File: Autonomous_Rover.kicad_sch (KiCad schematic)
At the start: 42 parts, among them J1 VL53L5X_R, J10 ESP32_R, J13 POWER, J14 BEAM_LIGHT, J15 MOTOR, J16 UART_5V, J17 UART_3V, J2 VEML7700, J3 VL53L5X_L, J4 HC-SR04_M, J5 VL53L5X_M, J7 BNO085, J9 ESP32_L, Q1 AO3400A, Q2 AO3400A, U1 AMS1117-3.3

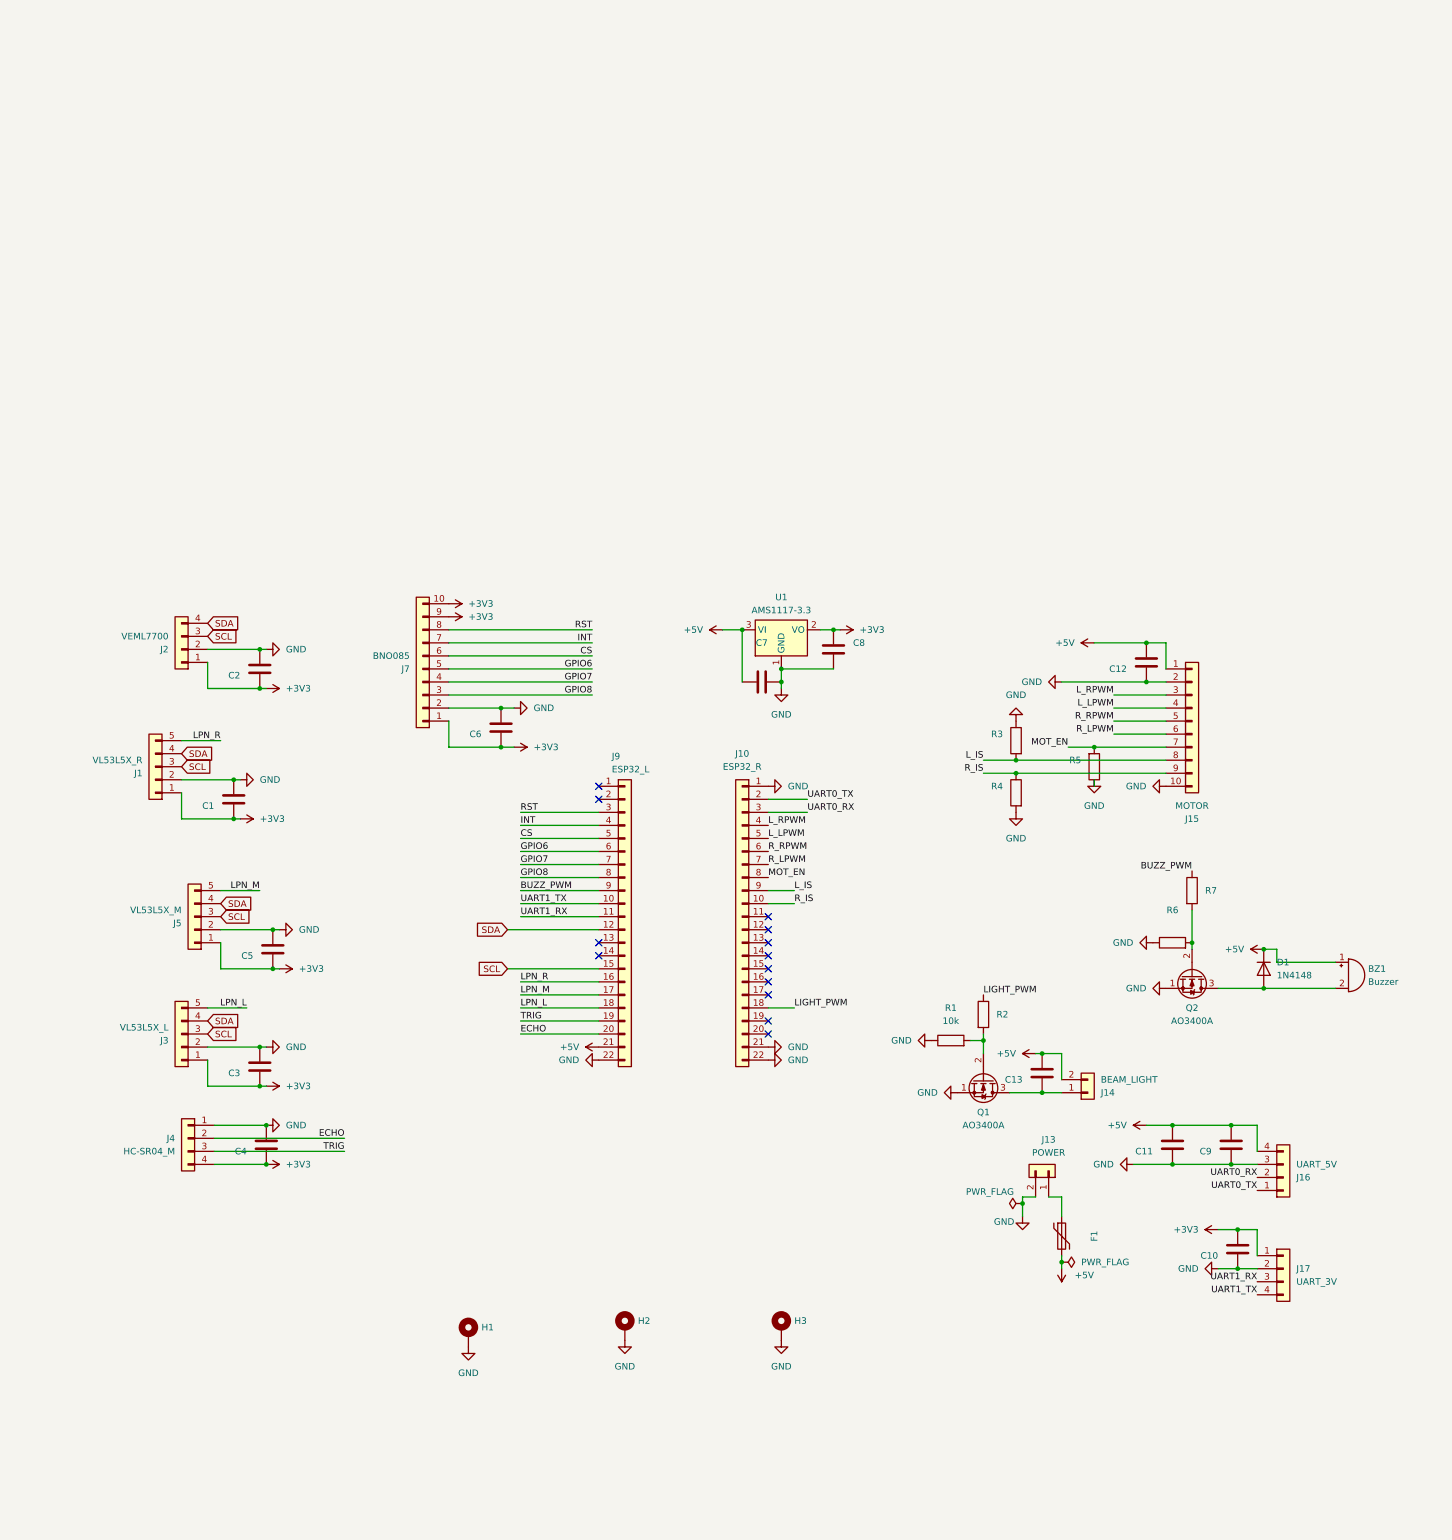
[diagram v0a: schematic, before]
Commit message: Reorganize Schematic
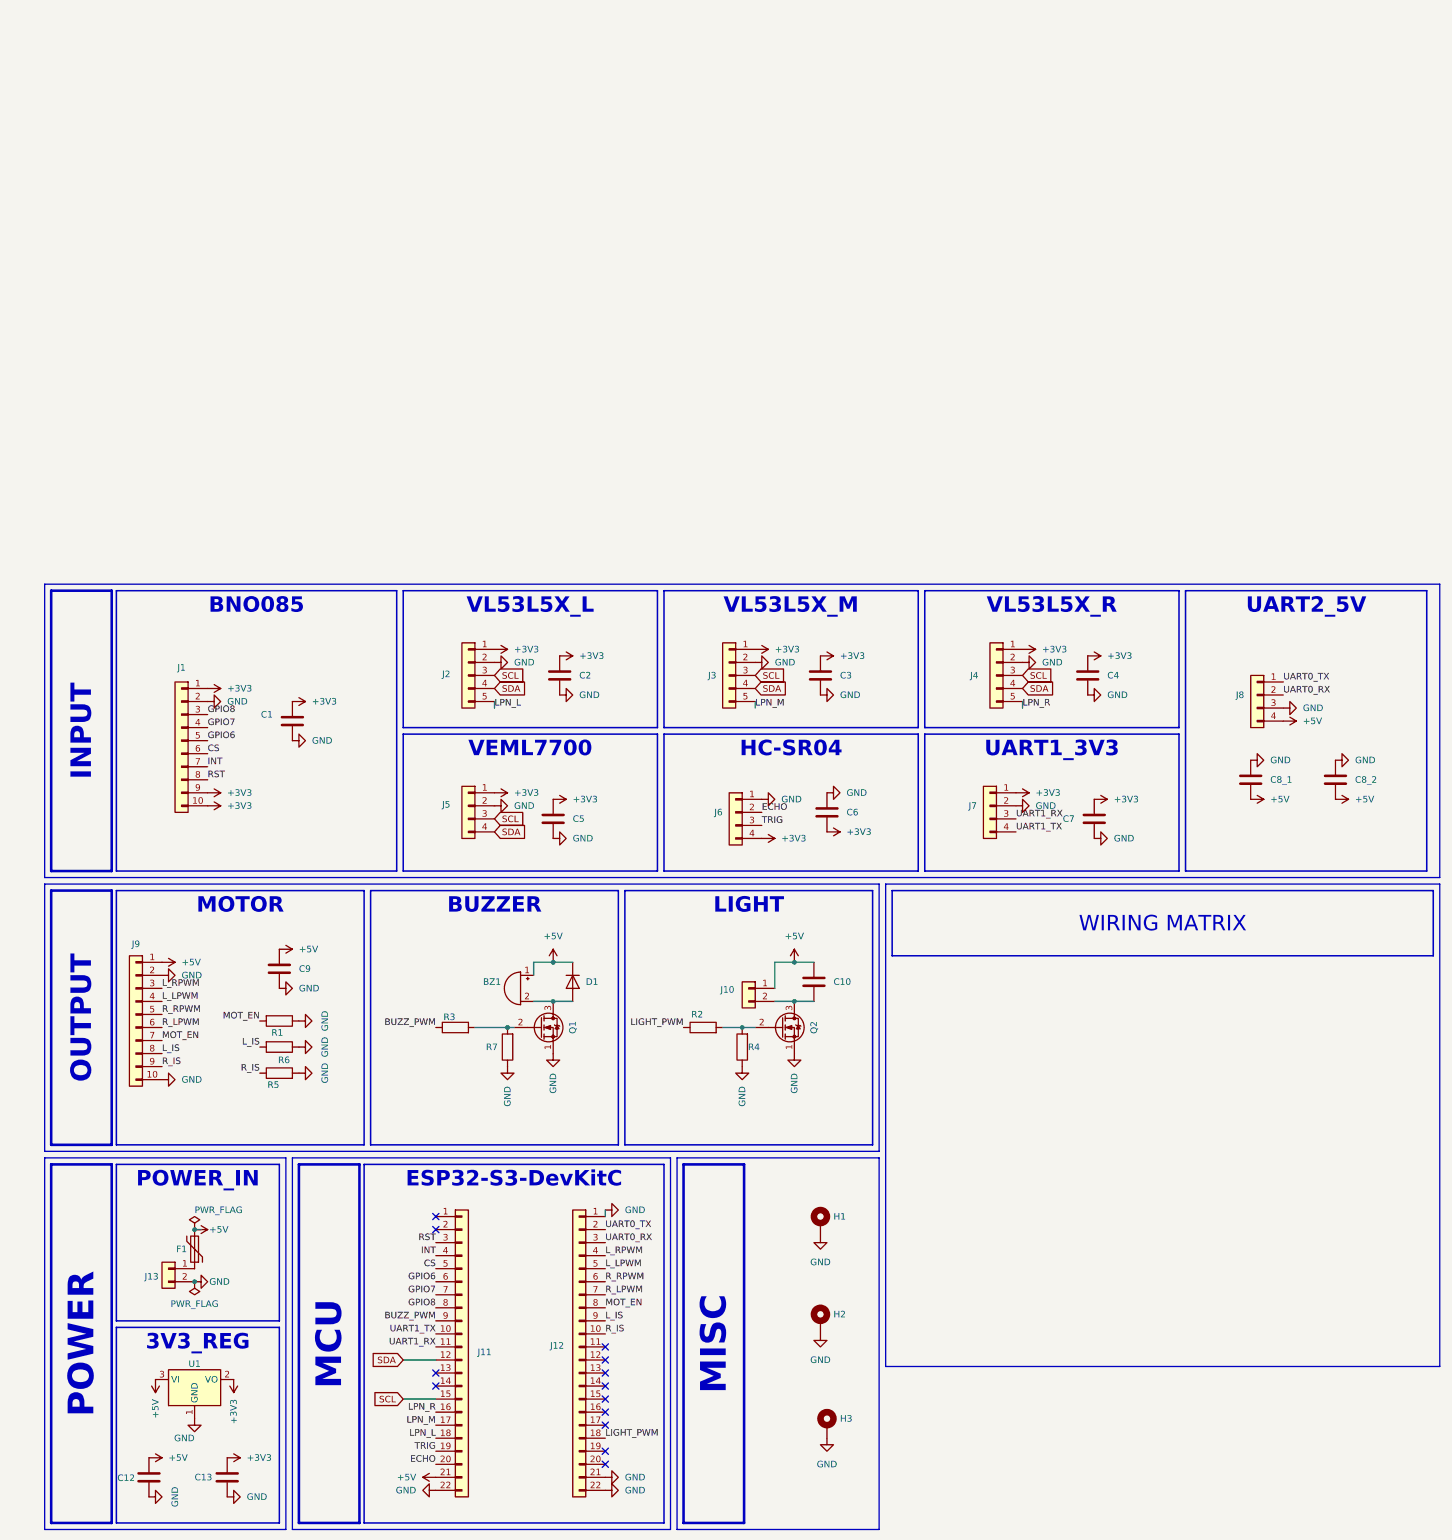
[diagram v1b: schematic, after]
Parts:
- removed C10: 100nF, Capacitor_SMD:C_0805_2012Metric, symbol Device:C
- removed C11, C8: 10uF, Capacitor_SMD:C_0805_2012Metric, symbol Device:C
- removed R3: 1k, Resistor_SMD:R_0805_2012Metric, symbol Device:R
- added C13, C8_2: 10uF, Capacitor_SMD:C_0805_2012Metric, symbol Device:C
- added C8_1: 100nF, Capacitor_SMD:C_0805_2012Metric, symbol Device:C
- added R6: 1k, Resistor_SMD:R_0805_2012Metric, symbol Device:R
- C12: value 100nF -> 10uF
- C7: value 10uF -> 100nF
- R4: value 1k -> 10k
- R5: value 10k -> 1k
- renumbered C13 to C10, J7 to J1, J14 to J10, J9 to J11, J10 to J12, J3 to J2, J5 to J3, J1 to J4, J2 to J5, J4 to J6, J17 to J7, J16 to J8, J15 to J9, R7 to R3, R6 to R7
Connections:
- net +3V3: now also C7.2, C13.1
- net +5V: now also C10.1, C12.1, J10.1 (Pin_1), C8_1.2, C8_2.2; no longer C10.2, C12.2, C7.1, J10.2 (Pin_2)
- net GND: now also C12.2, C7.1, R4.1, R5.2, C13.2, C8_1.1, C8_2.1, R6.1; no longer C12.1, C7.2, R4.2, R5.1
- net L_IS: now also R6.2
- net MOT_EN: now also R1.2; no longer R5.2
- net R_IS: now also R5.1; no longer R4.1
- net at R3.2, R7.2: now also Q1.2 (G); no longer Q2.2 (G)
- net at BZ1.2 (-), D1.2 (A): now also Q1.3 (D); no longer Q2.3 (D)
- new net: C10.2, J10.2 (Pin_2), Q2.3 (D)
- new net: Q2.2 (G), R2.2, R4.2
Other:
- moved on the sheet: BZ1, C10, F1, H1, H2, H3, J1, J10, J11, J12, J13, J2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

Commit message: Revision
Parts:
- removed BZ1: Buzzer, Buzzer_Beeper:Buzzer_12x9.5RM7.6, symbol Device:Buzzer
- removed C1, C2, C3, C4, C5, C6, C7, C8_1, C9: 100nF, Capacitor_SMD:C_0805_2012Metric, symbol Device:C
- removed C10, C12, C13, C8_2: 10uF, Capacitor_SMD:C_0805_2012Metric, symbol Device:C
- removed D1: 1N4148, Diode_SMD:D_SOD-123, symbol Diode:1N4148
- removed F1: 2.0A Hold / 3.5A Trip (16V+), Fuse:Fuse_2920_7451Metric, symbol Device:Polyfuse
- removed J1: BNO085, Connector_JST:JST_XH_B10B-XH-A_1x10_P2.50mm_Vertical, symbol Connector_Generic:Conn_01x10
- removed J10: BEAM_LIGHT, Connector_PinHeader_2.54mm:PinHeader_1x02_P2.54mm_Vertical, symbol Connector_Generic:Conn_01x02
- removed J13: POWER, Connector_Molex:Molex_Micro-Fit_3.0_43045-0200_2x01_P3.00mm_Horizontal, symbol Connector_Generic:Conn_01x02
- removed J2: VL53L5X_L, Connector_JST:JST_XH_B5B-XH-A_1x05_P2.50mm_Vertical, symbol Connector_Generic:Conn_01x05
- removed J3: VL53L5X_M, Connector_JST:JST_XH_B5B-XH-A_1x05_P2.50mm_Vertical, symbol Connector_Generic:Conn_01x05
- removed J4: VL53L5X_R, Connector_JST:JST_XH_B5B-XH-A_1x05_P2.50mm_Vertical, symbol Connector_Generic:Conn_01x05
- removed J5: VEML7700, Connector_JST:JST_XH_B4B-XH-A_1x04_P2.50mm_Vertical, symbol Connector_Generic:Conn_01x04
- removed J6: HC-SR04_M, Connector_JST:JST_XH_B4B-XH-A_1x04_P2.50mm_Vertical, symbol Connector_Generic:Conn_01x04
- removed J7: UART_3V, Connector_JST:JST_XH_B4B-XH-A_1x04_P2.50mm_Vertical, symbol Connector_Generic:Conn_01x04
- removed J8: UART_5V, Connector_JST:JST_XH_B4B-XH-A_1x04_P2.50mm_Vertical, symbol Connector_Generic:Conn_01x04
- removed J9: MOTOR, Connector_JST:JST_XH_B10B-XH-A_1x10_P2.50mm_Vertical, symbol Connector_Generic:Conn_01x10
- removed Q1, Q2: AO3400A, Package_TO_SOT_SMD:SOT-23, symbol Transistor_FET:2N7000
- removed R1, R4, R7: 10k, Resistor_SMD:R_0805_2012Metric, symbol Device:R
- removed R2, R3: 100, Resistor_SMD:R_0805_2012Metric, symbol Device:R
- removed R5, R6: 1k, Resistor_SMD:R_0805_2012Metric, symbol Device:R
- removed U1: AMS1117-3.3, Package_TO_SOT_SMD:SOT-223-3_TabPin2, symbol Regulator_Linear:AMS1117-3.3
- added C20: 22µF, Capacitor_SMD:C_0805_2012Metric_Pad1.18x1.45mm_HandSolder, symbol Device:C
- added C21, C28: 0.1µF, Capacitor_SMD:C_0805_2012Metric_Pad1.18x1.45mm_HandSolder, symbol Device:C
- added R19, R27: 10kΩ, Resistor_SMD:R_0805_2012Metric_Pad1.20x1.40mm_HandSolder, symbol Device:R
- added SW2: SW_SPDT, Button_Switch_SMD:SW_SPDT_Shouhan_MSK12C02, symbol Switch:SW_SPDT_custom
- renumbered J11 to J12, J12 to J13
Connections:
- net CS is gone; now on net UART1_TX: J12.5 (Pin_5)
- net ECHO is gone; now on net INT: J12.20 (Pin_20)
- net GPIO6 is gone; now on net UART1_RX: J12.6 (Pin_6)
- net GPIO8 is gone; now on net SDA: J12.8 (Pin_8)
- net L_IS is gone; now on net LIGHT_PWM: J13.9 (Pin_9)
- net R_IS is gone; now on net BUZZ_PWM: J13.10 (Pin_10)
- net +3V3: now also R27.1
- net +5V: now also C20.2, C21.2
- net BUZZ_PWM: no longer J12.9 (Pin_9)
- net GND: now also C20.1, C21.1, C28.1, R19.1, SW2.1 (A), SW2.SH
- net INT: no longer J12.4 (Pin_4)
- net LIGHT_PWM: no longer J13.18 (Pin_18)
- net L_LPWM: now also J13.4 (Pin_4); no longer J13.5 (Pin_5)
- net L_RPWM: now also J13.5 (Pin_5); no longer J13.4 (Pin_4)
- net MOT_EN: now also R19.2
- net R_LPWM: now also J13.6 (Pin_6); no longer J13.7 (Pin_7)
- net R_RPWM: now also J13.7 (Pin_7); no longer J13.6 (Pin_6)
- net SCL: now also J12.9 (Pin_9); no longer J12.15 (Pin_15)
- net SDA: no longer J12.12 (Pin_12)
- net UART1_RX: no longer J12.11 (Pin_11)
- net UART1_TX: no longer J12.10 (Pin_10)
- net D+: now reaches J13.19 (Pin_19)
- net D-: now reaches J13.20 (Pin_20)
- net GPIO7 renamed IIC_RST
- net LPN_L renamed SPICLK
- net LPN_M renamed MOSI
- net LPN_R renamed CS0
- net RST: no longer names the net of J12.3 (Pin_3)
- net TRIG renamed MISO
- new net LED1: J12.10 (Pin_10)
- new net LED2: J12.11 (Pin_11)
- new net MODE_SW: C28.2, J12.4 (Pin_4), R27.2, SW2.2 (B)
- new net SER_PWM1: J12.12 (Pin_12)
- new net SER_PWM2: J13.18 (Pin_18)
- new net SPI_RST: J12.15 (Pin_15)
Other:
- added sheet INPUT (Input.kicad_sch)
- added sheet OUTPUT (Output.kicad_sch)
- added sheet POWER (Power.kicad_sch)
- moved on the sheet: H1, H2, H3, J12, J13
